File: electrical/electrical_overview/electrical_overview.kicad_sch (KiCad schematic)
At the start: 11 parts, among them M1 Motor_Right_Front, M2 Motor_Right_Back, M3 Motor_Left_Front, M4 Motor_Left_Back, SW1 Start Button, U2 HC-SR04, U3 L298N, U4 L298N

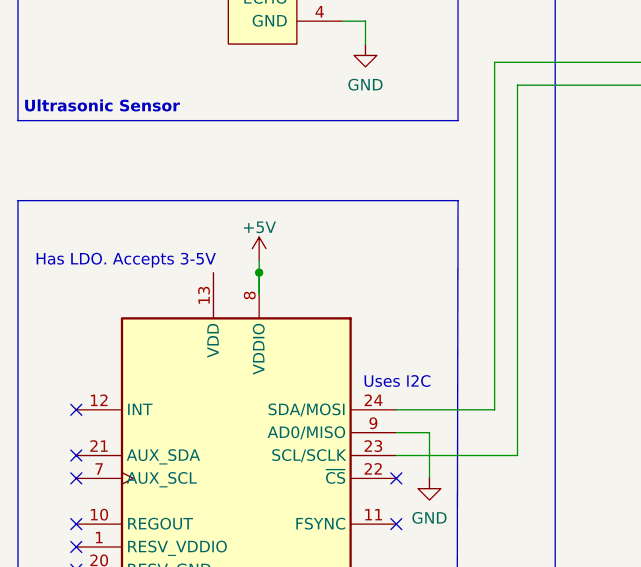
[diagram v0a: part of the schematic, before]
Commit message: Fix pins for IMU
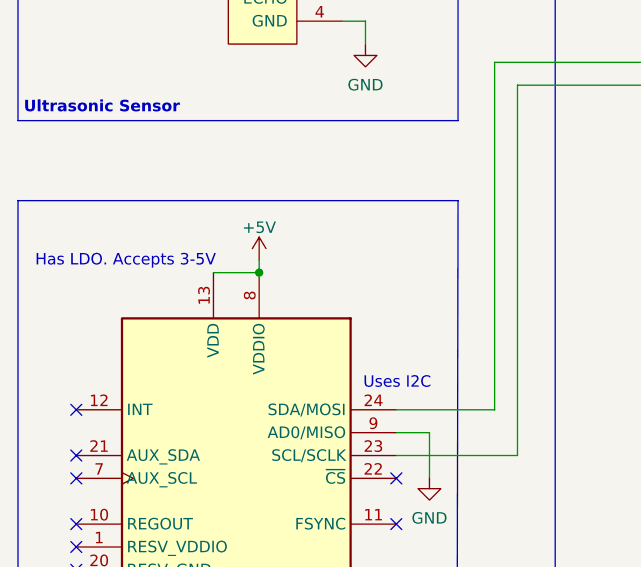
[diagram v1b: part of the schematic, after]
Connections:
- net +5V: now also U?.13 (VDD)
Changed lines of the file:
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@@
   (junction (at 99.06 140.208) (diameter 0) (color 0 0 0 0)
   )
+  (junction (at 49.657 87.376) (diameter 0) (color 0 0 0 0)
+  )
   (junction (at 99.06 142.748) (diameter 0) (color 0 0 0 0)
   )
   (junction (at 99.06 127.508) (diameter 0) (color 0 0 0 0)
-  )
-  (junction (at 49.657 87.376) (diameter 0) (color 0 0 0 0)
   )
   (junction (at 99.06 124.968) (diameter 0) (color 0 0 0 0)
@@
     (stroke (width 0) (type default) (color 0 0 0 0))
   )
+  (wire (pts (xy 44.577 87.376) (xy 49.657 87.376))
+    (stroke (width 0) (type default) (color 0 0 0 0))
+  )
   (polyline (pts (xy 22.86 142.113) (xy 22.86 79.375))
     (stroke (width 0) (type default) (color 0 0 0 0))
@@
     (stroke (width 0) (type default) (color 0 0 0 0))
   )
-  (wire (pts (xy 49.657 87.376) (xy 49.657 89.789))
-    (stroke (width 0) (type default) (color 0 0 0 0))
-  )
